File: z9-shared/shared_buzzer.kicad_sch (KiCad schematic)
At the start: 6 parts

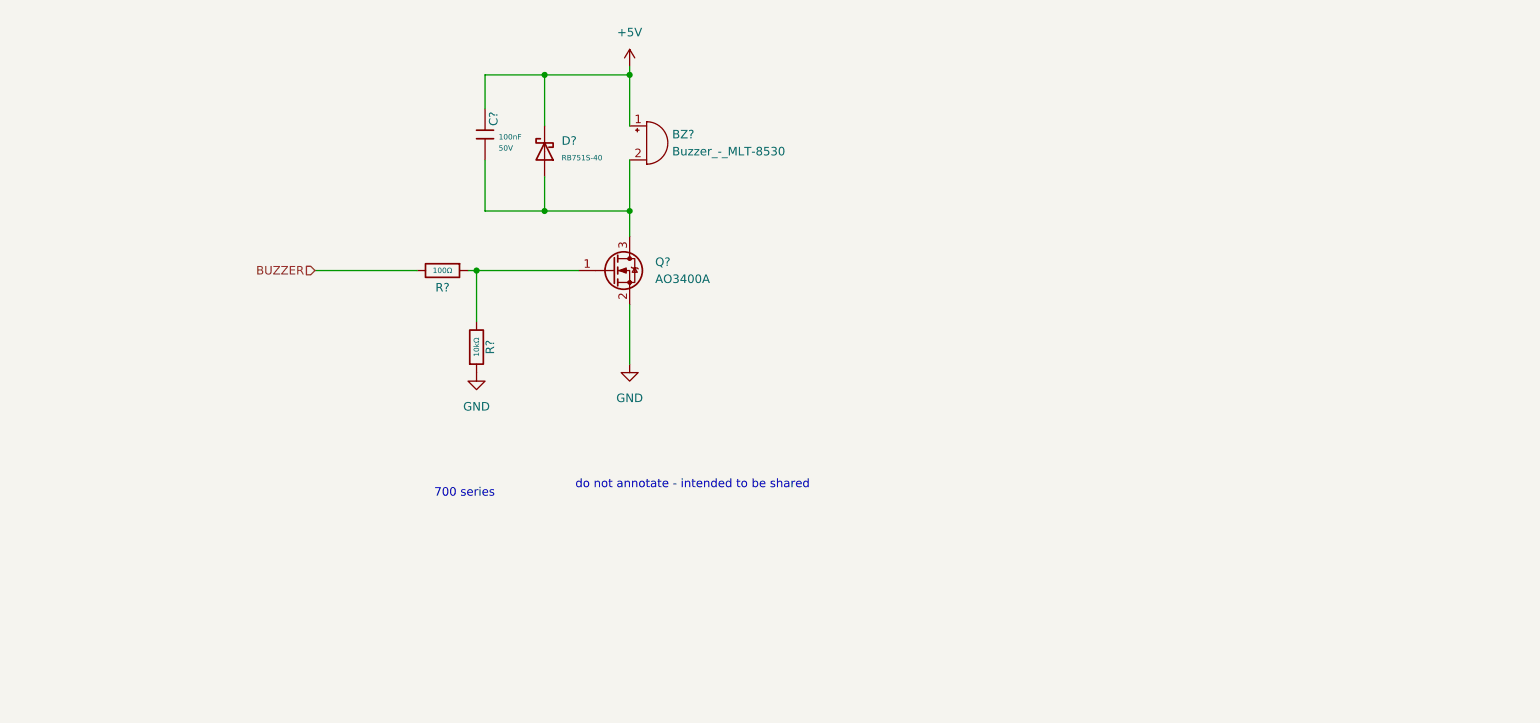
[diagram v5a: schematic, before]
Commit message: annotation issues on shared schematics
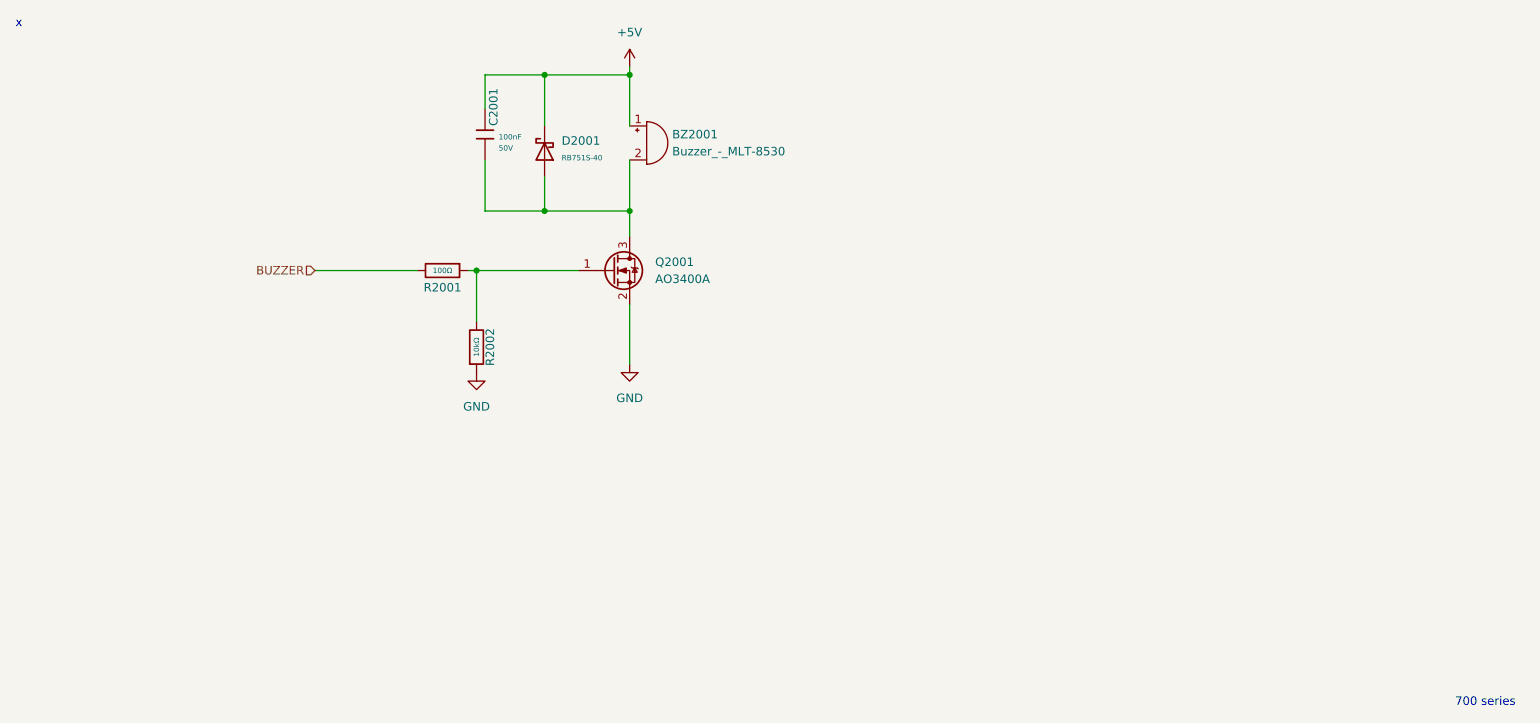
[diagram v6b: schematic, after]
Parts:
- gave numbers to parts that had none: 6
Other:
- note added: "x"
- note removed: "do not annotate - intended to be shared"
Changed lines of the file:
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@@
 		(title "l8")
 	)
-	(text "700 series "
+	(text "x"
 		(exclude_from_sim no)
-		(at 125.222 132.334 0)
+		(at 58.674 62.23 0)
 		(effects
 			(font
@@
 		)
 	)
-	(text "do not annotate - intended to be shared"
+	(text "700 series "
 		(exclude_from_sim no)
-		(at 159.258 131.064 0)
+		(at 277.622 163.576 0)
 		(effects
 			(font
@@
 		(dnp no)
 		(fields_autoplaced yes)
-		(property "Reference" "Q?"
+		(property "Reference" "Q2001"
 			(at 153.67 97.7899 0)
 			(effects
@@
 			(project "z9-pdm"
 				(path "/8d063f79-9282-4820-bcf4-1ff3c006cf08/c97401c5-7e03-4d93-a14f-f692468677b5"
-					(reference "Q?")
+					(reference "Q2001")
 					(unit 1)
 				)
@@
 		(dnp no)
 		(fields_autoplaced yes)
-		(property "Reference" "D?"
+		(property "Reference" "D2001"
 			(at 139.7 79.6924 0)
 			(effects
@@
 			(project "z9-pdm"
 				(path "/8d063f79-9282-4820-bcf4-1ff3c006cf08/c97401c5-7e03-4d93-a14f-f692468677b5"
-					(reference "D?")
+					(reference "D2001")
 					(unit 1)
 				)
@@
 		(dnp no)
 		(fields_autoplaced yes)
-		(property "Reference" "#PWR?"
+		(property "Reference" "#PWR02001"
 			(at 127 120.65 0)
 			(effects
@@
 			(project "z9-pdm"
 				(path "/8d063f79-9282-4820-bcf4-1ff3c006cf08/c97401c5-7e03-4d93-a14f-f692468677b5"
-					(reference "#PWR?")
+					(reference "#PWR02001")
 					(unit 1)
 				)
@@
 		(dnp no)
 		(fields_autoplaced yes)
-		(property "Reference" "#PWR?"
+		(property "Reference" "#PWR02002"
 			(at 149.86 72.39 0)
 			(effects
@@
 			(project "z9-pdm"
 				(path "/8d063f79-9282-4820-bcf4-1ff3c006cf08/c97401c5-7e03-4d93-a14f-f692468677b5"
-					(reference "#PWR?")
+					(reference "#PWR02002")
 					(unit 1)
 				)
@@
 		(on_board yes)
 		(dnp no)
-		(property "Reference" "C?"
+		(property "Reference" "C2001"
 			(at 129.54 77.47 90)
 			(effects
@@
 			(project "z9-pdm"
 				(path "/8d063f79-9282-4820-bcf4-1ff3c006cf08/c97401c5-7e03-4d93-a14f-f692468677b5"
-					(reference "C?")
+					(reference "C2001")
 					(unit 1)
 				)
@@
 		(dnp no)
 		(fields_autoplaced yes)
-		(property "Reference" "BZ?"
+		(property "Reference" "BZ2001"
 			(at 156.21 78.7399 0)
 			(effects
@@
 			(project "z9-pdm"
 				(path "/8d063f79-9282-4820-bcf4-1ff3c006cf08/c97401c5-7e03-4d93-a14f-f692468677b5"
-					(reference "BZ?")
+					(reference "BZ2001")
 					(unit 1)
 				)
@@
 		(on_board yes)
 		(dnp no)
-		(property "Reference" "R?"
+		(property "Reference" "R2002"
 			(at 129.032 110.49 90)
 			(effects
@@
 			(project "z9-pdm"
 				(path "/8d063f79-9282-4820-bcf4-1ff3c006cf08/c97401c5-7e03-4d93-a14f-f692468677b5"
-					(reference "R?")
+					(reference "R2002")
 					(unit 1)
 				)
@@
 		(on_board yes)
 		(dnp no)
-		(property "Reference" "R?"
+		(property "Reference" "R2001"
 			(at 121.92 101.6 90)
 			(effects
@@
 			(project "z9-pdm"
 				(path "/8d063f79-9282-4820-bcf4-1ff3c006cf08/c97401c5-7e03-4d93-a14f-f692468677b5"
-					(reference "R?")
+					(reference "R2001")
 					(unit 1)
 				)
@@
 		(dnp no)
 		(fields_autoplaced yes)
-		(property "Reference" "#PWR?"
+		(property "Reference" "#PWR02003"
 			(at 149.86 119.38 0)
 			(effects
@@
 			(project "z9-pdm"
 				(path "/8d063f79-9282-4820-bcf4-1ff3c006cf08/c97401c5-7e03-4d93-a14f-f692468677b5"
-					(reference "#PWR?")
+					(reference "#PWR02003")
 					(unit 1)
 				)

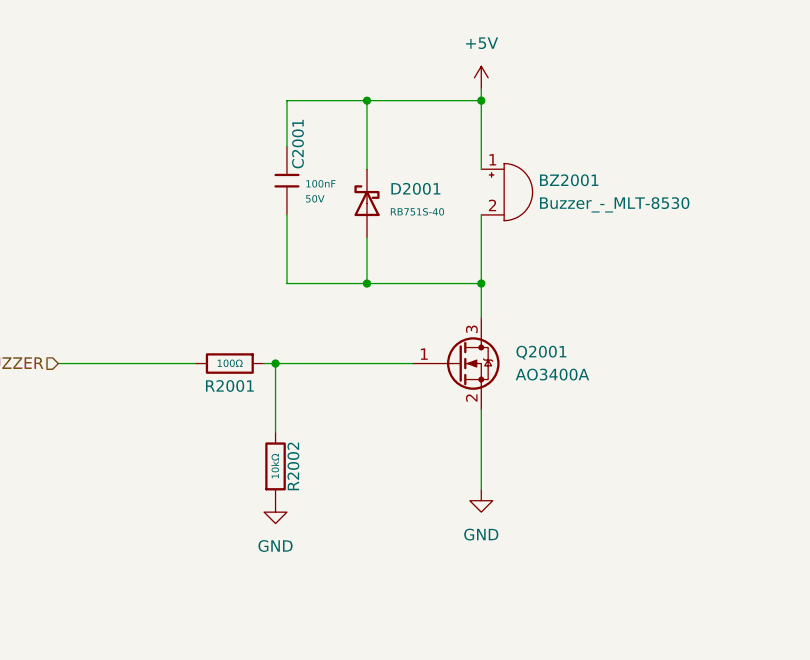
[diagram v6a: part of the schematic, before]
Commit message: reset shared chematics to correct series
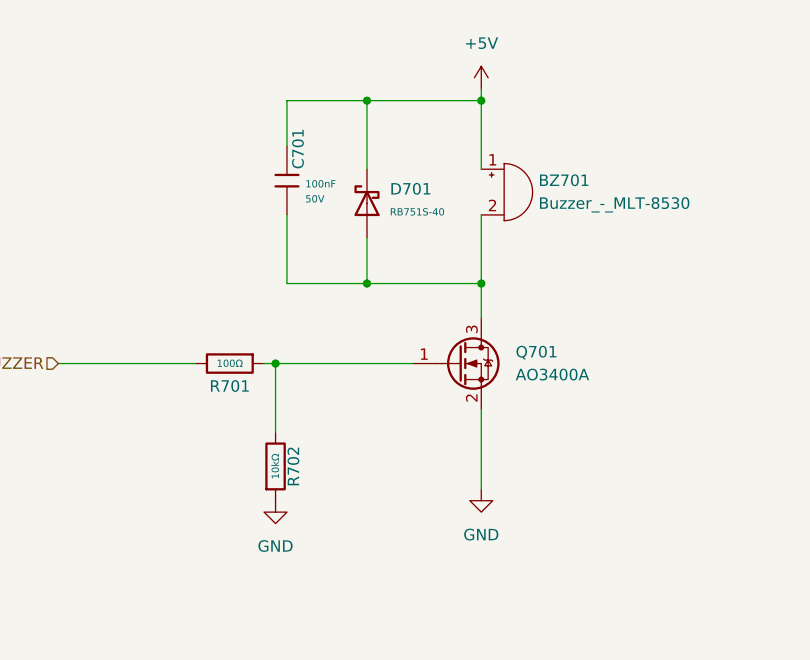
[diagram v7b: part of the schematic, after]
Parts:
- renumbered BZ2001 to BZ701, C2001 to C701, D2001 to D701, Q2001 to Q701, R2001 to R701, R2002 to R702
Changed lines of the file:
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@@
 		(dnp no)
 		(fields_autoplaced yes)
-		(property "Reference" "Q2001"
+		(property "Reference" "Q701"
 			(at 153.67 97.7899 0)
 			(effects
@@
 			(project "z9-shared"
 				(path "/09e08bdc-786f-4949-8afc-e02ddbe0502e/1a1ef1d0-80f8-40e1-820b-d8a0de9a6f67"
-					(reference "Q?")
+					(reference "Q701")
 					(unit 1)
 				)
@@
 		(dnp no)
 		(fields_autoplaced yes)
-		(property "Reference" "D2001"
+		(property "Reference" "D701"
 			(at 139.7 79.6924 0)
 			(effects
@@
 			(project "z9-shared"
 				(path "/09e08bdc-786f-4949-8afc-e02ddbe0502e/1a1ef1d0-80f8-40e1-820b-d8a0de9a6f67"
-					(reference "D?")
+					(reference "D701")
 					(unit 1)
 				)
@@
 		(dnp no)
 		(fields_autoplaced yes)
-		(property "Reference" "#PWR02001"
+		(property "Reference" "#PWR0701"
 			(at 127 120.65 0)
 			(effects
@@
 			(project "z9-shared"
 				(path "/09e08bdc-786f-4949-8afc-e02ddbe0502e/1a1ef1d0-80f8-40e1-820b-d8a0de9a6f67"
-					(reference "#PWR0103")
+					(reference "#PWR0701")
 					(unit 1)
 				)
@@
 		(dnp no)
 		(fields_autoplaced yes)
-		(property "Reference" "#PWR02002"
+		(property "Reference" "#PWR0702"
 			(at 149.86 72.39 0)
 			(effects
@@
 			(project "z9-shared"
 				(path "/09e08bdc-786f-4949-8afc-e02ddbe0502e/1a1ef1d0-80f8-40e1-820b-d8a0de9a6f67"
-					(reference "#PWR0102")
+					(reference "#PWR0702")
 					(unit 1)
 				)
@@
 		(on_board yes)
 		(dnp no)
-		(property "Reference" "C2001"
+		(property "Reference" "C701"
 			(at 129.54 77.47 90)
 			(effects
@@
 			(project "z9-shared"
 				(path "/09e08bdc-786f-4949-8afc-e02ddbe0502e/1a1ef1d0-80f8-40e1-820b-d8a0de9a6f67"
-					(reference "C?")
+					(reference "C701")
 					(unit 1)
 				)
@@
 		(dnp no)
 		(fields_autoplaced yes)
-		(property "Reference" "BZ2001"
+		(property "Reference" "BZ701"
 			(at 156.21 78.7399 0)
 			(effects
@@
 			(project "z9-shared"
 				(path "/09e08bdc-786f-4949-8afc-e02ddbe0502e/1a1ef1d0-80f8-40e1-820b-d8a0de9a6f67"
-					(reference "BZ?")
+					(reference "BZ701")
 					(unit 1)
 				)
@@
 		(on_board yes)
 		(dnp no)
-		(property "Reference" "R2002"
+		(property "Reference" "R702"
 			(at 129.032 110.49 90)
 			(effects
@@
 			(project "z9-shared"
 				(path "/09e08bdc-786f-4949-8afc-e02ddbe0502e/1a1ef1d0-80f8-40e1-820b-d8a0de9a6f67"
-					(reference "R?")
+					(reference "R702")
 					(unit 1)
 				)
@@
 		(on_board yes)
 		(dnp no)
-		(property "Reference" "R2001"
+		(property "Reference" "R701"
 			(at 121.92 101.6 90)
 			(effects
@@
 			(project "z9-shared"
 				(path "/09e08bdc-786f-4949-8afc-e02ddbe0502e/1a1ef1d0-80f8-40e1-820b-d8a0de9a6f67"
-					(reference "R?")
+					(reference "R701")
 					(unit 1)
 				)
@@
 		(dnp no)
 		(fields_autoplaced yes)
-		(property "Reference" "#PWR02003"
+		(property "Reference" "#PWR0703"
 			(at 149.86 119.38 0)
 			(effects
@@
 			(project "z9-shared"
 				(path "/09e08bdc-786f-4949-8afc-e02ddbe0502e/1a1ef1d0-80f8-40e1-820b-d8a0de9a6f67"
-					(reference "#PWR0101")
-					(unit 1)
-				)
+					(reference "#PWR0703")
+					(unit 1)
+				)
